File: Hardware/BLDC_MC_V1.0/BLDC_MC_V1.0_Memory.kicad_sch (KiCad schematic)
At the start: 9 parts

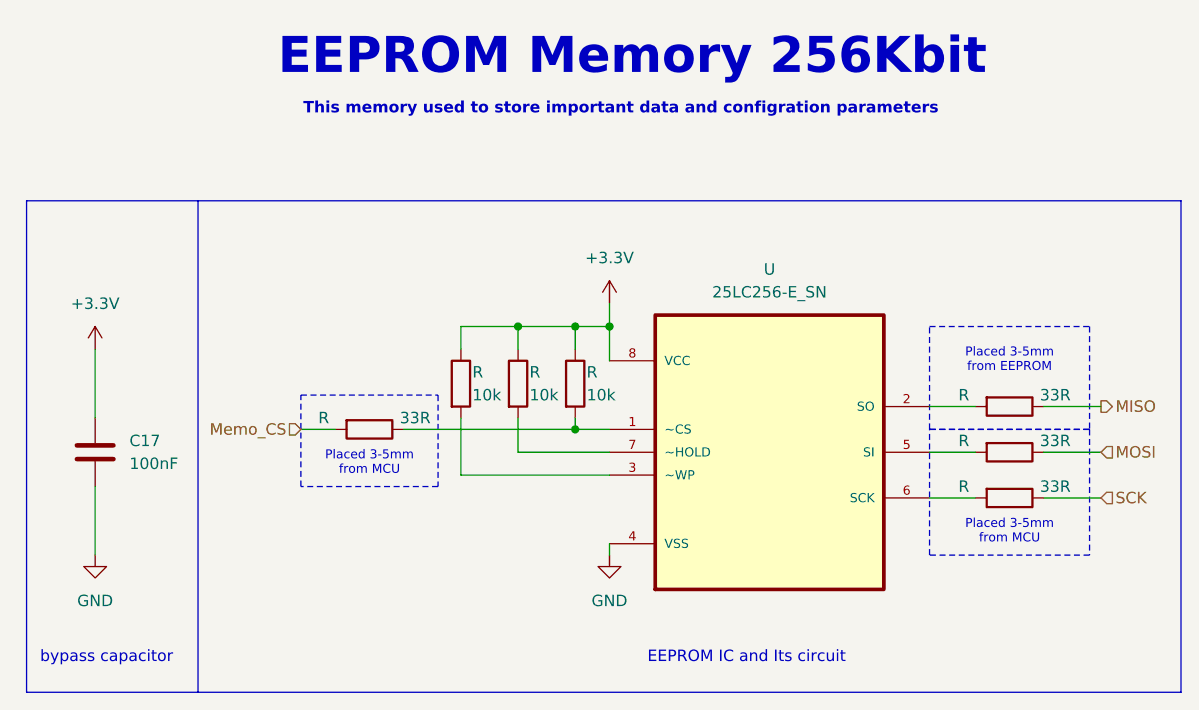
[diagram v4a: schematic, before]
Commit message: Edit the sch of the project by adding the hall sensor sheet and interface with the MCU sheet and annotate the components in memory sheet
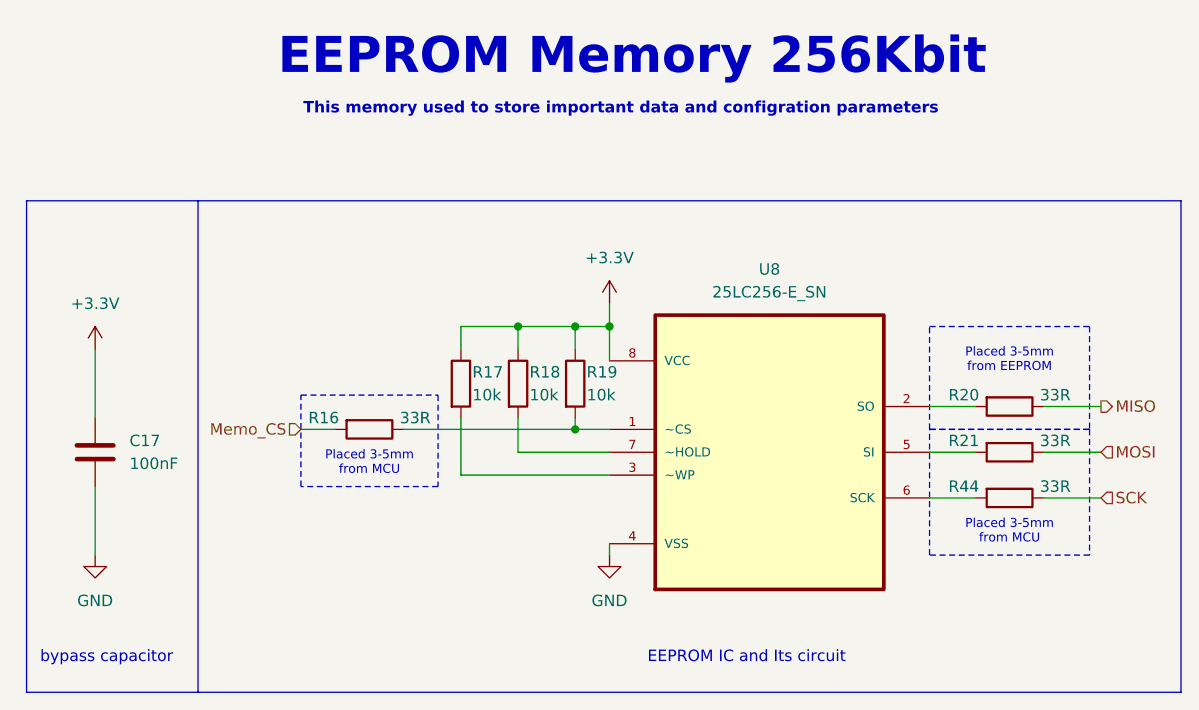
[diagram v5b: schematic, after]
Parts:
- renumbered R to R16, R to R17, R to R18, R to R19, R to R20, R to R21, R to R44, U to U8
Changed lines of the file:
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@@
 		(dnp no)
 		(fields_autoplaced yes)
-		(property "Reference" "#PWR"
+		(property "Reference" "#PWR092"
 			(at 144.78 115.57 0)
 			(effects
@@
 		(pin "1"
 		)
-		(instances)
+		(instances
+			(project "BLDC_MC_V1.0"
+				(path "/e34fda66-7244-4ac9-bbf7-3725f03e688f/bcfa60d7-9b39-4a60-8e0a-1c9d768132f8"
+					(reference "#PWR092")
+					(unit 1)
+				)
+			)
+		)
 	)
 	(symbol
@@
 		(on_board yes)
 		(dnp no)
-		(property "Reference" "R"
+		(property "Reference" "R44"
 			(at 184.15 101.6 90)
 			(effects
@@
 		(pin "1"
 		)
-		(instances)
+		(instances
+			(project "BLDC_MC_V1.0"
+				(path "/e34fda66-7244-4ac9-bbf7-3725f03e688f/bcfa60d7-9b39-4a60-8e0a-1c9d768132f8"
+					(reference "R44")
+					(unit 1)
+				)
+			)
+		)
 	)
 	(symbol
@@
 		(on_board yes)
 		(dnp no)
-		(property "Reference" "R"
+		(property "Reference" "R21"
 			(at 184.15 96.52 90)
 			(effects
@@
 		(pin "1"
 		)
-		(instances)
+		(instances
+			(project "BLDC_MC_V1.0"
+				(path "/e34fda66-7244-4ac9-bbf7-3725f03e688f/bcfa60d7-9b39-4a60-8e0a-1c9d768132f8"
+					(reference "R21")
+					(unit 1)
+				)
+			)
+		)
 	)
 	(symbol
@@
 		(on_board yes)
 		(dnp no)
-		(property "Reference" "R"
+		(property "Reference" "R17"
 			(at 129.54 88.9 0)
 			(effects
@@
 		(pin "2"
 		)
-		(instances)
+		(instances
+			(project "BLDC_MC_V1.0"
+				(path "/e34fda66-7244-4ac9-bbf7-3725f03e688f/bcfa60d7-9b39-4a60-8e0a-1c9d768132f8"
+					(reference "R17")
+					(unit 1)
+				)
+			)
+		)
 	)
 	(symbol
@@
 		(on_board yes)
 		(dnp no)
-		(property "Reference" "R"
+		(property "Reference" "R16"
 			(at 113.03 93.98 90)
 			(effects
@@
 		(pin "1"
 		)
-		(instances)
+		(instances
+			(project "BLDC_MC_V1.0"
+				(path "/e34fda66-7244-4ac9-bbf7-3725f03e688f/bcfa60d7-9b39-4a60-8e0a-1c9d768132f8"
+					(reference "R16")
+					(unit 1)
+				)
+			)
+		)
 	)
 	(symbol
@@
 		(dnp no)
 		(fields_autoplaced yes)
-		(property "Reference" "#PWR"
+		(property "Reference" "#PWR032"
 			(at 87.63 115.57 0)
 			(effects
@@
 		(pin "1"
 		)
-		(instances)
+		(instances
+			(project "BLDC_MC_V1.0"
+				(path "/e34fda66-7244-4ac9-bbf7-3725f03e688f/bcfa60d7-9b39-4a60-8e0a-1c9d768132f8"
+					(reference "#PWR032")
+					(unit 1)
+				)
+			)
+		)
 	)
 	(symbol
@@
 		(on_board yes)
 		(dnp no)
-		(property "Reference" "R"
+		(property "Reference" "R18"
 			(at 135.89 88.9 0)
 			(effects
@@
 		(pin "2"
 		)
-		(instances)
+		(instances
+			(project "BLDC_MC_V1.0"
+				(path "/e34fda66-7244-4ac9-bbf7-3725f03e688f/bcfa60d7-9b39-4a60-8e0a-1c9d768132f8"
+					(reference "R18")
+					(unit 1)
+				)
+			)
+		)
 	)
 	(symbol
@@
 		(on_board yes)
 		(dnp no)
-		(property "Reference" "R"
+		(property "Reference" "R20"
 			(at 184.15 91.44 90)
 			(effects
@@
 		(pin "1"
 		)
-		(instances)
+		(instances
+			(project "BLDC_MC_V1.0"
+				(path "/e34fda66-7244-4ac9-bbf7-3725f03e688f/bcfa60d7-9b39-4a60-8e0a-1c9d768132f8"
+					(reference "R20")
+					(unit 1)
+				)
+			)
+		)
 	)
 	(symbol
@@
 		(dnp no)
 		(fields_autoplaced yes)
-		(property "Reference" "#PWR"
+		(property "Reference" "#PWR031"
 			(at 87.63 90.17 0)
 			(effects
@@
 		(pin "1"
 		)
-		(instances)
+		(instances
+			(project "BLDC_MC_V1.0"
+				(path "/e34fda66-7244-4ac9-bbf7-3725f03e688f/bcfa60d7-9b39-4a60-8e0a-1c9d768132f8"
+					(reference "#PWR031")
+					(unit 1)
+				)
+			)
+		)
 	)
 	(symbol
@@
 		(on_board yes)
 		(dnp no)
-		(property "Reference" "R"
+		(property "Reference" "R19"
 			(at 142.24 88.9 0)
 			(effects
@@
 		(pin "2"
 		)
-		(instances)
+		(instances
+			(project "BLDC_MC_V1.0"
+				(path "/e34fda66-7244-4ac9-bbf7-3725f03e688f/bcfa60d7-9b39-4a60-8e0a-1c9d768132f8"
+					(reference "R19")
+					(unit 1)
+				)
+			)
+		)
 	)
 	(symbol
@@
 		(dnp no)
 		(fields_autoplaced yes)
-		(property "Reference" "U"
+		(property "Reference" "U8"
 			(at 162.56 77.47 0)
 			(effects
@@
 		(pin "1"
 		)
-		(instances)
+		(instances
+			(project "BLDC_MC_V1.0"
+				(path "/e34fda66-7244-4ac9-bbf7-3725f03e688f/bcfa60d7-9b39-4a60-8e0a-1c9d768132f8"
+					(reference "U8")
+					(unit 1)
+				)
+			)
+		)
 	)
 	(symbol
@@
 		(dnp no)
 		(fields_autoplaced yes)
-		(property "Reference" "#PWR"
+		(property "Reference" "#PWR086"
 			(at 144.78 85.09 0)
 			(effects
@@
 		(pin "1"
 		)
-		(instances)
+		(instances
+			(project "BLDC_MC_V1.0"
+				(path "/e34fda66-7244-4ac9-bbf7-3725f03e688f/bcfa60d7-9b39-4a60-8e0a-1c9d768132f8"
+					(reference "#PWR086")
+					(unit 1)
+				)
+			)
+		)
 	)
 )

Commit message: Add voltage sensor to measure the 3 phase voltage of inverter bridge
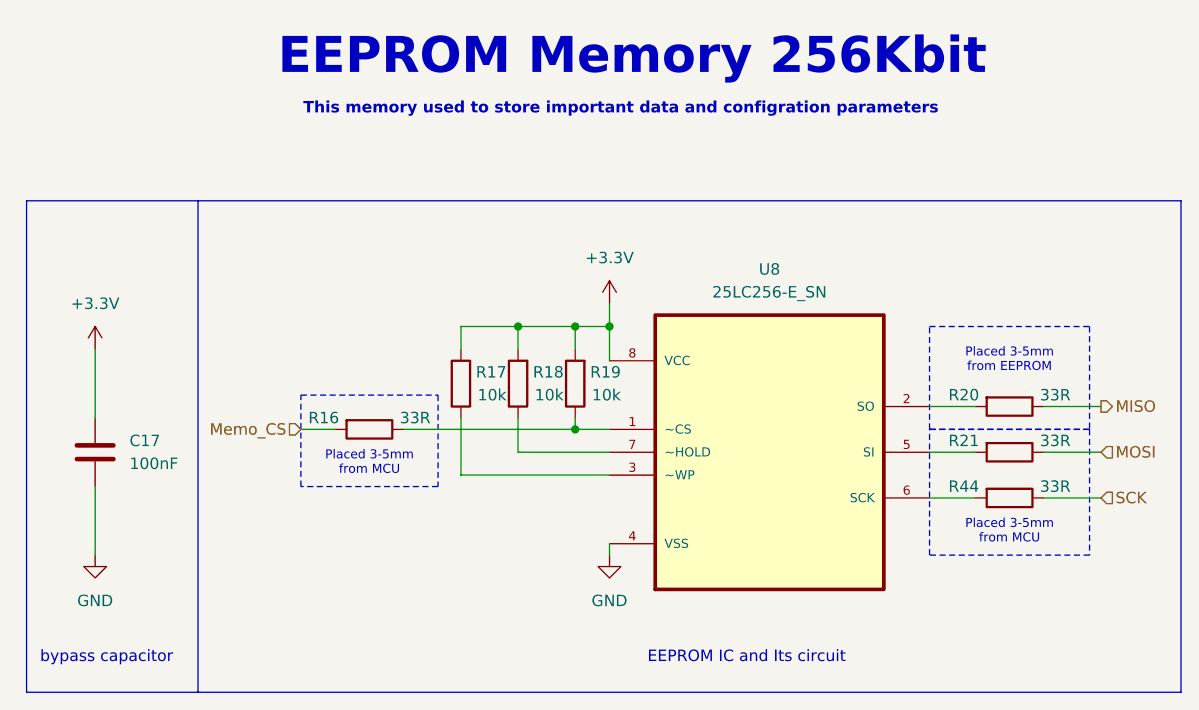
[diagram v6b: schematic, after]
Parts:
- R17, R18, R19: LCSC_PN C98220 -> C95204; MP RC0603FR-0710KL -> RT0603BRD0710KL
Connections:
- net +3.3V: now also R17.2, R18.2, R19.2; no longer R17.1, R18.1, R19.1
- net at U8.3 (~WP): now also R17.1; no longer R17.2
- net at R16.1, U8.1 (~CS): now also R19.1; no longer R19.2
- net at U8.7 (~HOLD): now also R18.1; no longer R18.2
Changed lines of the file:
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@@
+	(symbol
+		(lib_id "Device:R")
+		(at 128.27 90.17 180)
+		(unit 1)
+		(exclude_from_sim no)
+		(in_bom yes)
+		(on_board yes)
+		(dnp no)
+		(property "Reference" "R17"
+			(at 133.35 88.9 0)
+			(effects
+				(font
+					(size 1.27 1.27)
+				)
+				(justify left)
+			)
+		)
+		(property "Value" "10k"
+			(at 133.35 91.44 0)
+			(effects
+				(font
+					(size 1.27 1.27)
+				)
+				(justify left)
+			)
+		)
+		(property "Footprint" "Resistor_SMD:R_0603_1608Metric"
+			(at 130.048 90.17 90)
+			(effects
+				(font
+					(size 1.27 1.27)
+				)
+				(hide yes)
+			)
+		)
+		(property "Datasheet" "https://www.lcsc.com/datasheet/C95204.pdf"
+			(at 128.27 90.17 0)
+			(effects
+				(font
+					(size 1.27 1.27)
+				)
+				(hide yes)
+			)
+		)
+		(property "Description" "Resistor"
+			(at 128.27 90.17 0)
+			(effects
+				(font
+					(size 1.27 1.27)
+				)
+				(hide yes)
+			)
+		)
+		(property "LCSC_PN" "C95204"
+			(at 128.27 90.17 0)
+			(effects
+				(font
+					(size 1.27 1.27)
+				)
+				(hide yes)
+			)
+		)
+		(property "MP" "RT0603BRD0710KL"
+			(at 128.27 90.17 0)
+			(effects
+				(font
+					(size 1.27 1.27)
+				)
+				(hide yes)
+			)
+		)
+		(property "Assembled" "Yes"
+			(at 128.27 90.17 0)
+			(effects
+				(font
+					(size 1.27 1.27)
+				)
+				(hide yes)
+			)
+		)
+		(pin "1"
+		)
+		(pin "2"
+		)
+		(instances
+			(project "BLDC_MC_V1.0"
+				(path "/e34fda66-7244-4ac9-bbf7-3725f03e688f/bcfa60d7-9b39-4a60-8e0a-1c9d768132f8"
+					(reference "R17")
+					(unit 1)
+				)
+			)
+		)
+	)
 	(symbol
 		(lib_id "Device:R")
@@
 	(symbol
 		(lib_id "Device:R")
-		(at 128.27 90.17 0)
-		(unit 1)
-		(exclude_from_sim no)
-		(in_bom yes)
-		(on_board yes)
-		(dnp no)
-		(property "Reference" "R17"
-			(at 129.54 88.9 0)
+		(at 134.62 90.17 180)
+		(unit 1)
+		(exclude_from_sim no)
+		(in_bom yes)
+		(on_board yes)
+		(dnp no)
+		(property "Reference" "R18"
+			(at 139.7 88.9 0)
 			(effects
 				(font
@@
 		)
 		(property "Value" "10k"
-			(at 129.54 91.44 0)
+			(at 139.7 91.44 0)
 			(effects
 				(font
@@
 		)
 		(property "Footprint" "Resistor_SMD:R_0603_1608Metric"
-			(at 126.492 90.17 90)
-			(effects
-				(font
-					(size 1.27 1.27)
-				)
-				(hide yes)
-			)
-		)
-		(property "Datasheet" "https://www.lcsc.com/datasheet/C98220.pdf"
-			(at 128.27 90.17 0)
+			(at 136.398 90.17 90)
+			(effects
+				(font
+					(size 1.27 1.27)
+				)
+				(hide yes)
+			)
+		)
+		(property "Datasheet" "https://www.lcsc.com/datasheet/C95204.pdf"
+			(at 134.62 90.17 0)
 			(effects
 				(font
@@
 		)
 		(property "Description" "Resistor"
-			(at 128.27 90.17 0)
-			(effects
-				(font
-					(size 1.27 1.27)
-				)
-				(hide yes)
-			)
-		)
-		(property "LCSC_PN" "C98220"
-			(at 128.27 90.17 0)
-			(effects
-				(font
-					(size 1.27 1.27)
-				)
-				(hide yes)
-			)
-		)
-		(property "MP" "RC0603FR-0710KL"
-			(at 128.27 90.17 0)
+			(at 134.62 90.17 0)
+			(effects
+				(font
+					(size 1.27 1.27)
+				)
+				(hide yes)
+			)
+		)
+		(property "LCSC_PN" "C95204"
+			(at 134.62 90.17 0)
+			(effects
+				(font
+					(size 1.27 1.27)
+				)
+				(hide yes)
+			)
+		)
+		(property "MP" "RT0603BRD0710KL"
+			(at 134.62 90.17 0)
 			(effects
 				(font
@@
 		)
 		(property "Assembled" "Yes"
-			(at 128.27 90.17 0)
+			(at 134.62 90.17 0)
 			(effects
 				(font
@@
 			(project "BLDC_MC_V1.0"
 				(path "/e34fda66-7244-4ac9-bbf7-3725f03e688f/bcfa60d7-9b39-4a60-8e0a-1c9d768132f8"
-					(reference "R17")
+					(reference "R18")
 					(unit 1)
 				)
@@
 	)
 	(symbol
-		(lib_id "Device:R")
-		(at 134.62 90.17 0)
-		(unit 1)
-		(exclude_from_sim no)
-		(in_bom yes)
-		(on_board yes)
-		(dnp no)
-		(property "Reference" "R18"
-			(at 135.89 88.9 0)
-			(effects
-				(font
-					(size 1.27 1.27)
-				)
-				(justify left)
-			)
-		)
-		(property "Value" "10k"
-			(at 135.89 91.44 0)
-			(effects
-				(font
-					(size 1.27 1.27)
-				)
-				(justify left)
-			)
-		)
-		(property "Footprint" "Resistor_SMD:R_0603_1608Metric"
-			(at 132.842 90.17 90)
-			(effects
-				(font
-					(size 1.27 1.27)
-				)
-				(hide yes)
-			)
-		)
-		(property "Datasheet" "https://www.lcsc.com/datasheet/C98220.pdf"
-			(at 134.62 90.17 0)
-			(effects
-				(font
-					(size 1.27 1.27)
-				)
-				(hide yes)
-			)
-		)
-		(property "Description" "Resistor"
-			(at 134.62 90.17 0)
-			(effects
-				(font
-					(size 1.27 1.27)
-				)
-				(hide yes)
-			)
-		)
-		(property "LCSC_PN" "C98220"
-			(at 134.62 90.17 0)
-			(effects
-				(font
-					(size 1.27 1.27)
-				)
-				(hide yes)
-			)
-		)
-		(property "MP" "RC0603FR-0710KL"
-			(at 134.62 90.17 0)
-			(effects
-				(font
-					(size 1.27 1.27)
-				)
-				(hide yes)
-			)
-		)
-		(property "Assembled" "Yes"
-			(at 134.62 90.17 0)
-			(effects
-				(font
-					(size 1.27 1.27)
-				)
-				(hide yes)
-			)
-		)
-		(pin "1"
-		)
-		(pin "2"
-		)
-		(instances
-			(project "BLDC_MC_V1.0"
-				(path "/e34fda66-7244-4ac9-bbf7-3725f03e688f/bcfa60d7-9b39-4a60-8e0a-1c9d768132f8"
-					(reference "R18")
-					(unit 1)
-				)
-			)
-		)
-	)
-	(symbol
 		(lib_id "Device:C")
 		(at 87.63 97.79 0)
@@
 	(symbol
 		(lib_id "Device:R")
-		(at 140.97 90.17 0)
+		(at 140.97 90.17 180)
 		(unit 1)
 		(exclude_from_sim no)
@@
 		(dnp no)
 		(property "Reference" "R19"
-			(at 142.24 88.9 0)
+			(at 146.05 88.9 0)
 			(effects
 				(font
@@
 		)
 		(property "Value" "10k"
-			(at 142.24 91.44 0)
+			(at 146.05 91.44 0)
 			(effects
 				(font
@@
 		)
 		(property "Footprint" "Resistor_SMD:R_0603_1608Metric"
-			(at 139.192 90.17 90)
-			(effects
-				(font
-					(size 1.27 1.27)
-				)
-				(hide yes)
-			)
-		)
-		(property "Datasheet" "https://www.lcsc.com/datasheet/C98220.pdf"
+			(at 142.748 90.17 90)
+			(effects
+				(font
+					(size 1.27 1.27)
+				)
+				(hide yes)
+			)
+		)
+		(property "Datasheet" "https://www.lcsc.com/datasheet/C95204.pdf"
 			(at 140.97 90.17 0)
 			(effects
@@
 			)
 		)
-		(property "LCSC_PN" "C98220"
+		(property "LCSC_PN" "C95204"
 			(at 140.97 90.17 0)
 			(effects
@@
 			)
 		)
-		(property "MP" "RC0603FR-0710KL"
+		(property "MP" "RT0603BRD0710KL"
 			(at 140.97 90.17 0)
 			(effects

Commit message: Adjust the connections between sheets
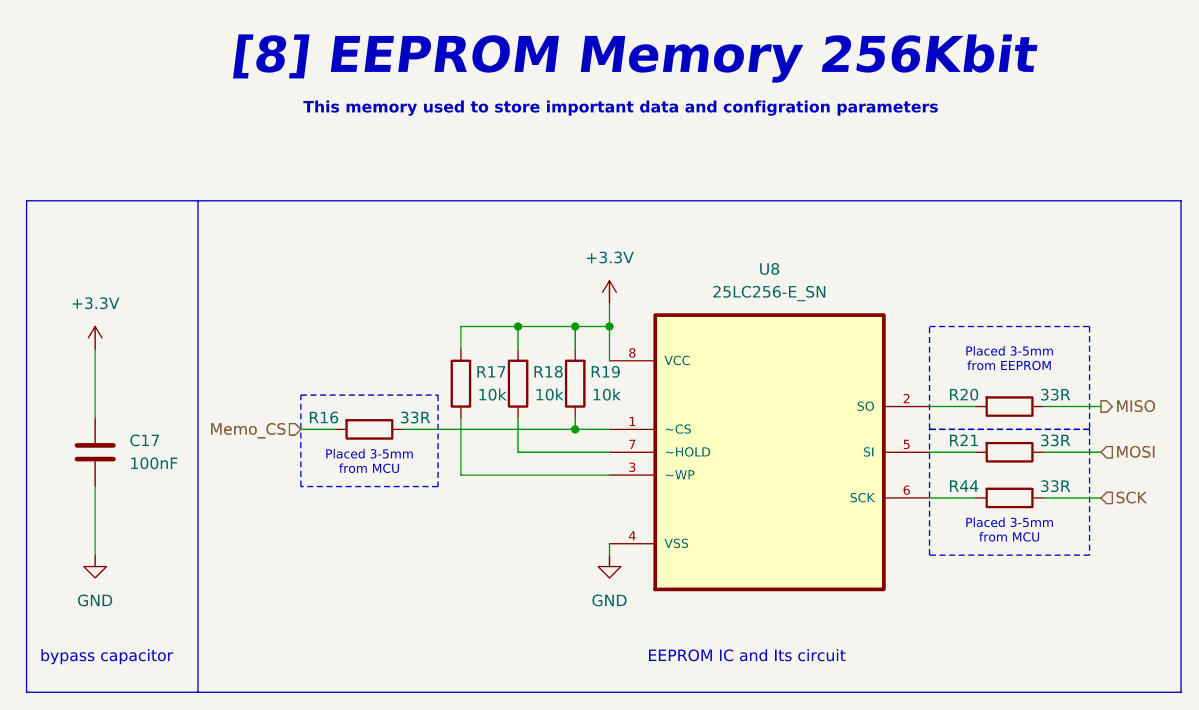
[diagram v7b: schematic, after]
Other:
- note added: "[8] EEPROM Memory 256Kbit"
- note removed: "EEPROM Memory 256Kbit"
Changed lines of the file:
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@@
 		)
 	)
-	(text "EEPROM Memory 256Kbit \n\n"
+	(text "[8] EEPROM Memory 256Kbit \n\n"
 		(exclude_from_sim no)
 		(at 147.32 57.15 0)
@@
 				(thickness 0.8)
 				(bold yes)
+				(italic yes)
 				(color 132 0 0 1)
 			)

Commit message: Solve all errors and wornings in project
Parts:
- U8: footprint 25LC256-E_SN:SOIC127P600X175-8N -> BLDC_Motor_Driver_Components_Footprint:SOIC127P599X175-8N
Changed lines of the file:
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@@
 			)
 		)
-		(property "Datasheet" "https://www.lcsc.com/datasheet/C95204.pdf"
+		(property "Datasheet" "~"
 			(at 128.27 90.17 0)
 			(effects
@@
 			)
 		)
-		(property "Datasheet" "https://www.lcsc.com/datasheet/C108661.pdf"
+		(property "Datasheet" "~"
 			(at 189.23 102.87 0)
 			(effects
@@
 			)
 		)
-		(property "Datasheet" "https://www.lcsc.com/datasheet/C108661.pdf"
+		(property "Datasheet" "~"
 			(at 189.23 97.79 0)
 			(effects
@@
 			)
 		)
-		(property "Datasheet" "https://www.lcsc.com/datasheet/C95204.pdf"
+		(property "Datasheet" "~"
 			(at 134.62 90.17 0)
 			(effects
@@
 			)
 		)
-		(property "Datasheet" "https://www.lcsc.com/datasheet/C108661.pdf"
+		(property "Datasheet" "~"
 			(at 118.11 95.25 0)
 			(effects
@@
 			)
 		)
-		(property "Datasheet" "https://www.lcsc.com/datasheet/C28233.pdf"
+		(property "Datasheet" "~"
 			(at 87.63 97.79 0)
 			(effects
@@
 			)
 		)
-		(property "Datasheet" "https://www.lcsc.com/datasheet/C108661.pdf"
+		(property "Datasheet" "~"
 			(at 189.23 92.71 0)
 			(effects
@@
 			)
 		)
-		(property "Datasheet" "https://www.lcsc.com/datasheet/C95204.pdf"
+		(property "Datasheet" "~"
 			(at 140.97 90.17 0)
 			(effects
@@
 			)
 		)
-		(property "Footprint" "25LC256-E_SN:SOIC127P600X175-8N"
+		(property "Footprint" "BLDC_Motor_Driver_Components_Footprint:SOIC127P599X175-8N"
 			(at 162.56 97.79 0)
 			(effects
